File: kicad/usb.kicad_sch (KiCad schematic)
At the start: 0 parts

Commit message: added xu316
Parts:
- added U10: XU316-1024-QF60B-C24, QFN_F60B-C24_XMO, symbol openmic:XU316-1024-QF60B-C24
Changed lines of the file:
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@@
 	(generator_version "9.0")
 	(paper "A4")
+	(symbol
+		(lib_id "openmic:XU316-1024-QF60B-C24")
+		(at 123.19 57.15 0)
+		(unit 1)
+		(exclude_from_sim no)
+		(in_bom yes)
+		(on_board yes)
+		(dnp no)
+		(fields_autoplaced yes)
+		(property "Reference" "U10"
+			(at 151.13 46.99 0)
+			(effects
+				(font
+					(size 1.524 1.524)
+				)
+			)
+		)
+		(property "Value" "XU316-1024-QF60B-C24"
+			(at 151.13 49.53 0)
+			(effects
+				(font
+					(size 1.524 1.524)
+				)
+			)
+		)
+		(property "Footprint" "QFN_F60B-C24_XMO"
+			(at 123.19 57.15 0)
+			(effects
+				(font
+					(size 1.27 1.27)
+					(italic yes)
+				)
+				(hide yes)
+			)
+		)
+		(property "Datasheet" "XU316-1024-QF60B-C24"
+			(at 123.19 57.15 0)
+			(effects
+				(font
+					(size 1.27 1.27)
+					(italic yes)
+				)
+				(hide yes)
+			)
+		)
+		(property "Description" ""
+			(at 123.19 57.15 0)
+			(effects
+				(font
+					(size 1.27 1.27)
+				)
+				(hide yes)
+			)
+		)
+		(pin "17"
+		)
+		(pin "14"
+		)
+		(pin "16"
+		)
+		(pin "15"
+		)
+		(pin "56"
+		)
+		(pin "57"
+		)
+		(pin "58"
+		)
+		(pin "53"
+		)
+		(pin "54"
+		)
+		(pin "55"
+		)
+		(pin "59"
+		)
+		(pin "60"
+		)
+		(pin "39"
+		)
+		(pin "40"
+		)
+		(pin "38"
+		)
+		(pin "37"
+		)
+		(pin "35"
+		)
+		(pin "36"
+		)
+		(pin "33"
+		)
+		(pin "34"
+		)
+		(pin "25"
+		)
+		(pin "24"
+		)
+		(pin "23"
+		)
+		(pin "22"
+		)
+		(pin "6"
+		)
+		(pin "5"
+		)
+		(pin "13"
+		)
+		(pin "12"
+		)
+		(pin "1"
+		)
+		(pin "4"
+		)
+		(pin "3"
+		)
+		(pin "2"
+		)
+		(pin "10"
+		)
+		(pin "11"
+		)
+		(pin "9"
+		)
+		(pin "8"
+		)
+		(pin "7"
+		)
+		(pin "31"
+		)
+		(pin "30"
+		)
+		(pin "29"
+		)
+		(pin "28"
+		)
+		(pin "27"
+		)
+		(pin "26"
+		)
+		(pin "65"
+		)
+		(pin "32"
+		)
+		(pin "61"
+		)
+		(pin "62"
+		)
+		(pin "63"
+		)
+		(pin "64"
+		)
+		(pin "41"
+		)
+		(pin "52"
+		)
+		(pin "51"
+		)
+		(pin "50"
+		)
+		(pin "49"
+		)
+		(pin "48"
+		)
+		(pin "47"
+		)
+		(pin "46"
+		)
+		(pin "45"
+		)
+		(pin "44"
+		)
+		(pin "43"
+		)
+		(pin "42"
+		)
+		(pin "19"
+		)
+		(pin "18"
+		)
+		(pin "21"
+		)
+		(pin "20"
+		)
+		(instances
+			(project "openmic"
+				(path "/84faeadc-8b12-4a66-a17f-5c56e5923fb8/ac4749a9-b66d-4a3a-8eaa-94f1fe3c6a5c"
+					(reference "U10")
+					(unit 1)
+				)
+			)
+		)
+	)
 )

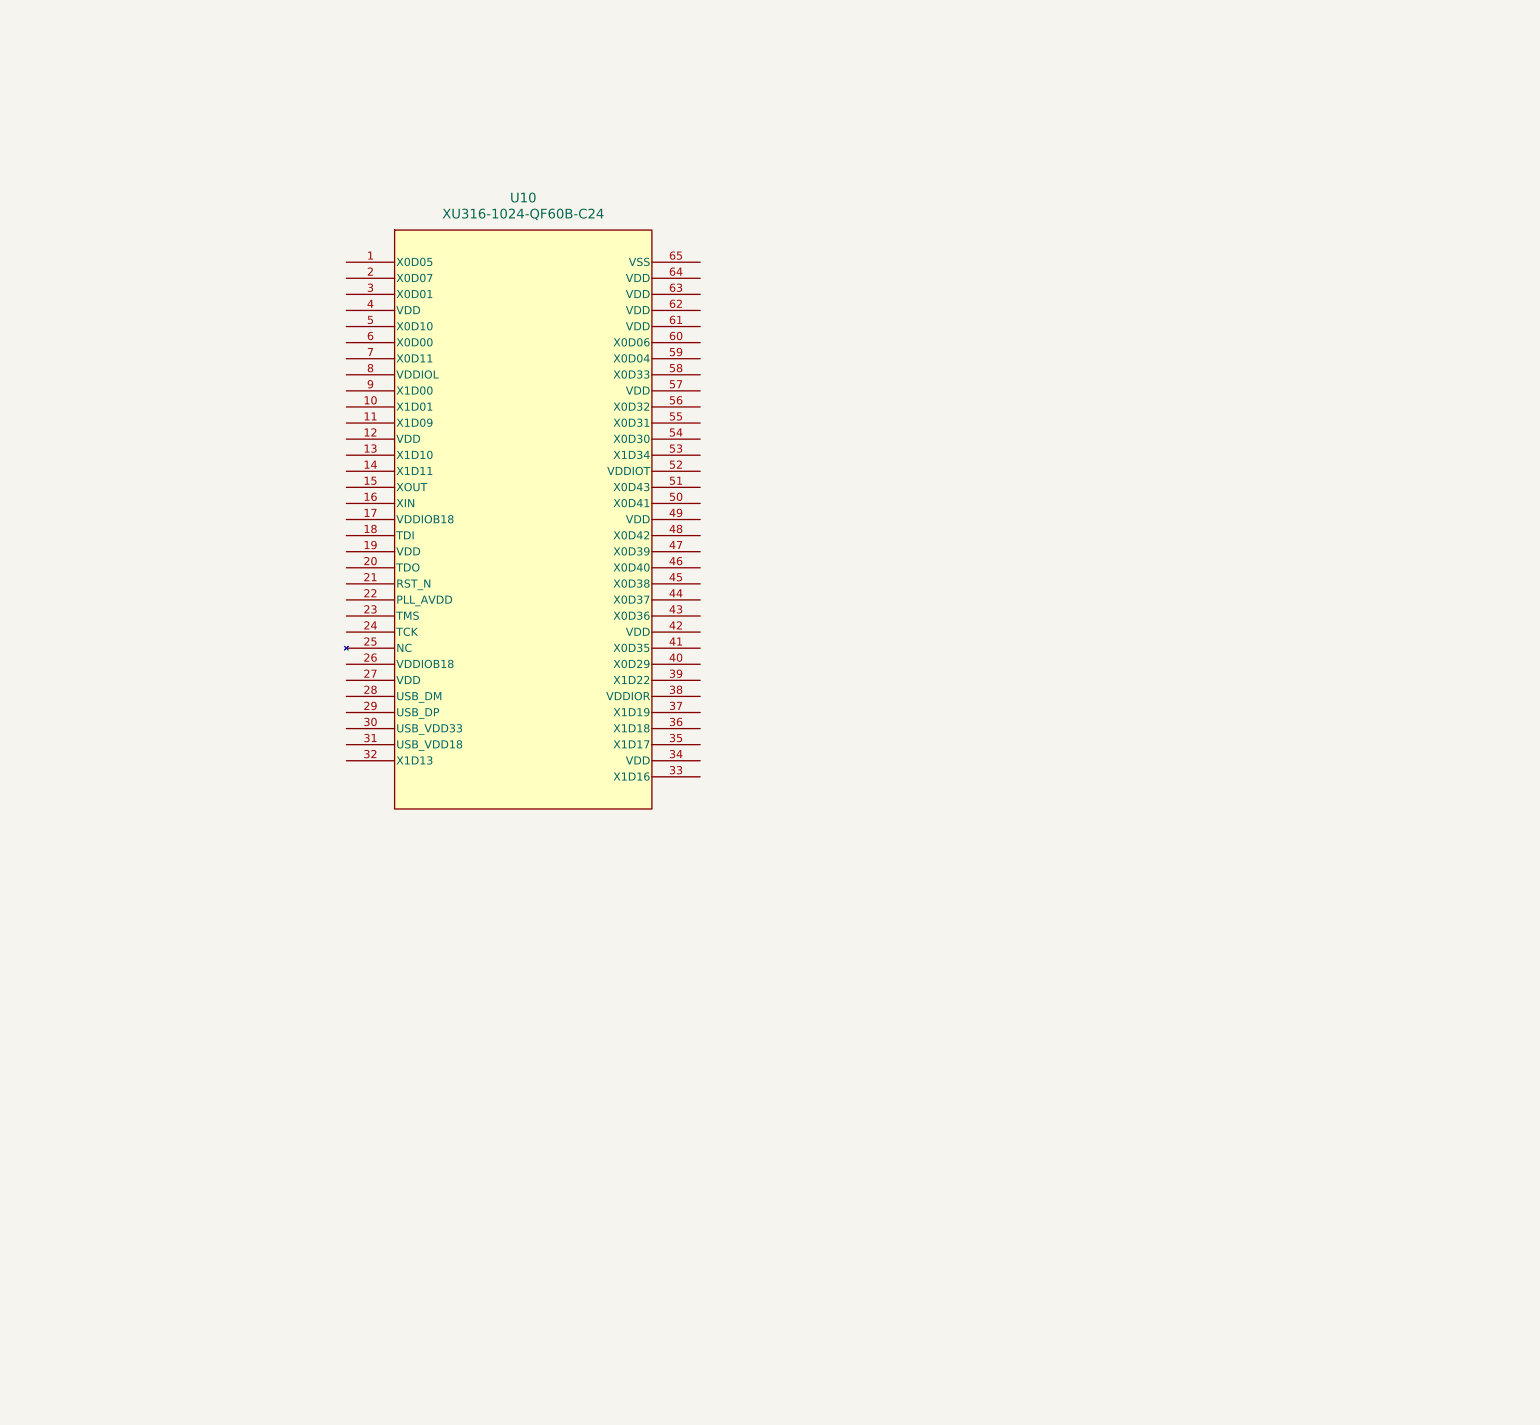
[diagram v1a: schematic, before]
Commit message: XU316 as usb device
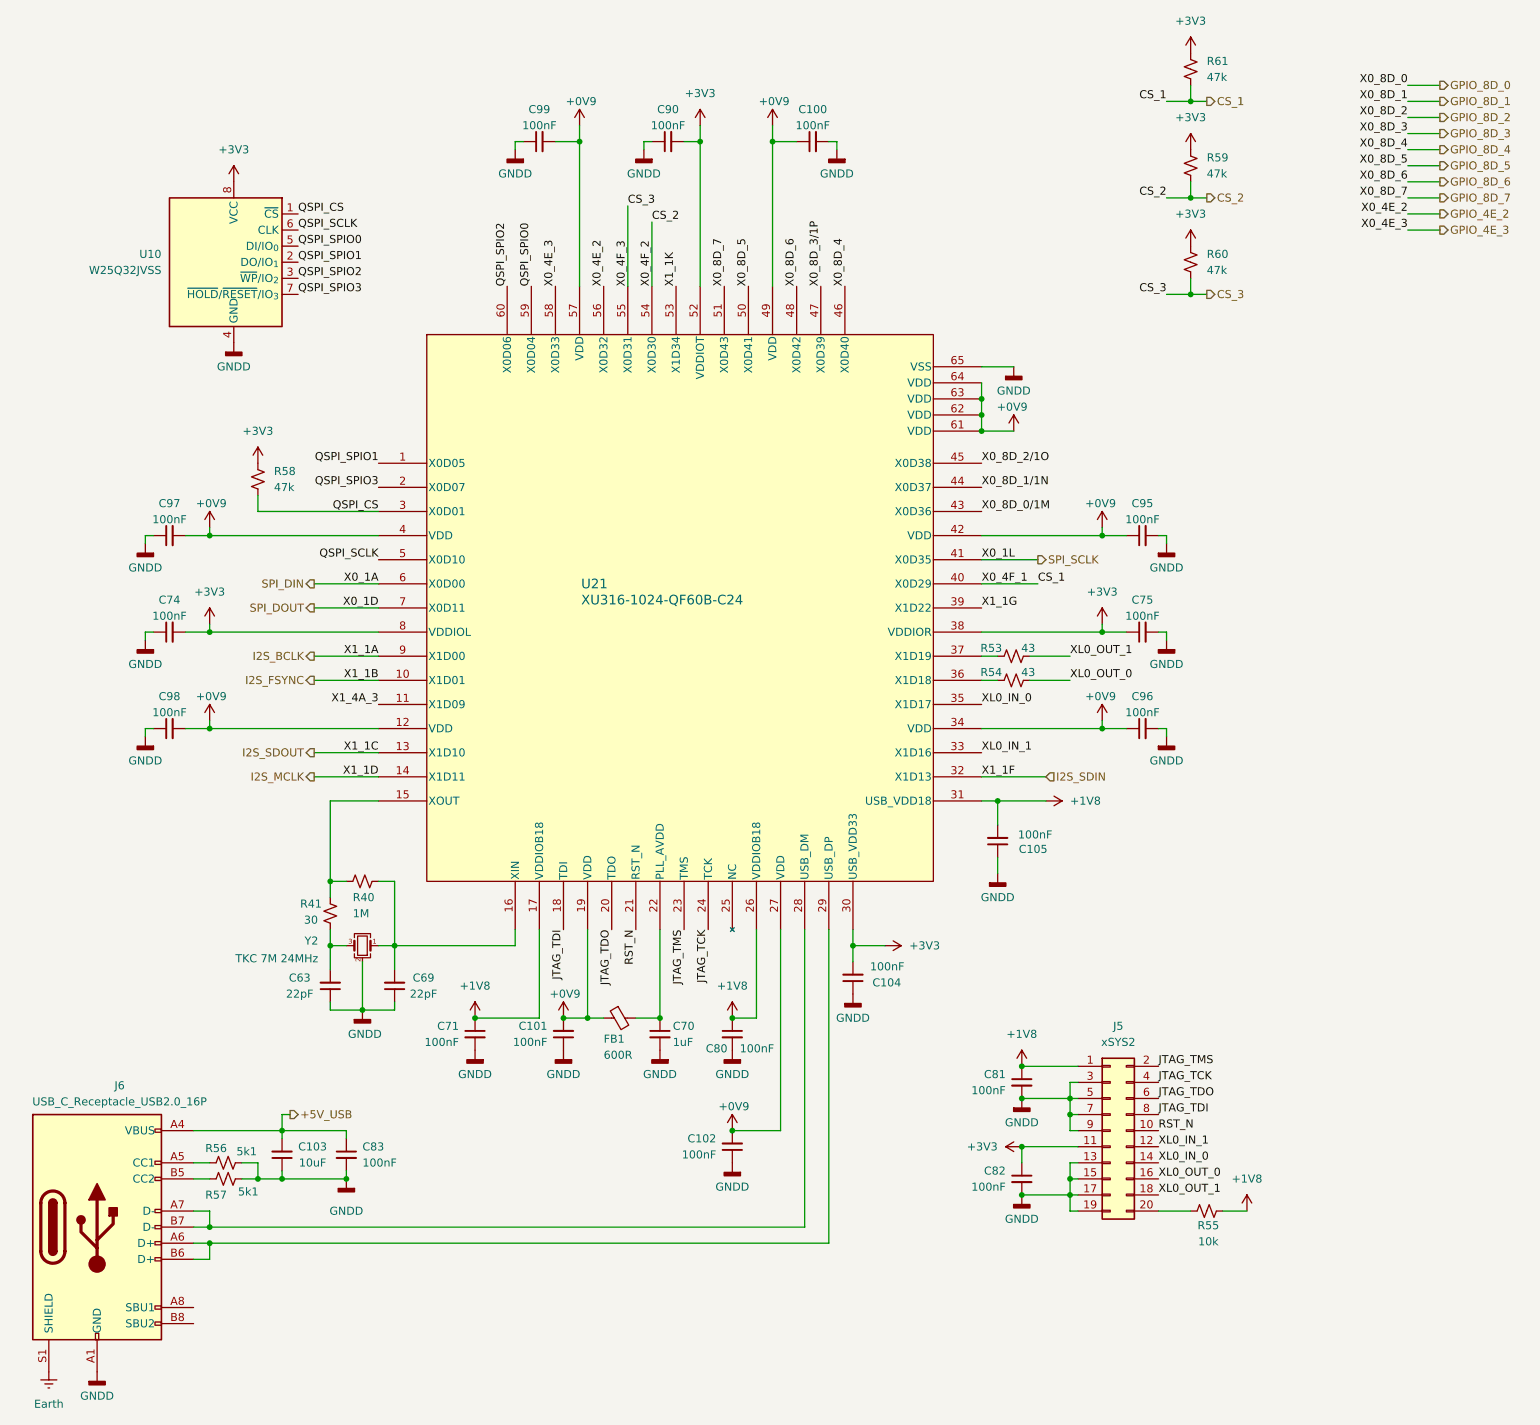
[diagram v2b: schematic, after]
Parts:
- removed U10: XU316-1024-QF60B-C24, QFN_F60B-C24_XMO, symbol openmic:XU316-1024-QF60B-C24
- added C100, C101, C102, C104, C105, C71, C74, C75, C80, C81, C82, C83, C90, C95, C96, C97, C98, C99: 100nF, symbol Device:C_Small
- added C103: 10uF, symbol Device:C_Small
- added C63, C69: 22pF, symbol Device:C_Small
- added C70: 1uF, symbol Device:C_Small
- added FB1: 600R, symbol Device:FerriteBead_Small
- added J5: xSYS2, symbol Connector_Generic:Conn_02x10_Odd_Even
- added J6: USB_C_Receptacle_USB2.0_16P, symbol Connector:USB_C_Receptacle_USB2.0_16P
- added R40: 1M, symbol Device:R_Small_US
- added R41: 30, symbol Device:R_Small_US
- added R53, R54: 43, symbol Device:R_Small_US
- added R55: 10k, symbol Device:R_Small_US
- added R56, R57: 5k1, symbol Device:R_Small_US
- added R58, R59, R60, R61: 47k, symbol Device:R_Small_US
- added U10: W25Q32JVSS, Package_SO:SOIC-8_5.3x5.3mm_P1.27mm, symbol Memory_Flash:W25Q32JVSS
- added U21: XU316-1024-QF60B-C24, QFN_F60B-C24_XMO, symbol openmic:XU316-1024-QF60B-C24_1
- added Y2: TKC 7M 24MHz, symbol Device:Crystal_GND24_Small
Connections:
- new net: C63.2, R41.1, Y2.3
- new net: J5.20 (Pin_20), R55.2
- new net: R40.1, R41.2, U21.15 (XOUT)
- new net: C69.2, R40.2, U21.16 (XIN), Y2.1
- new net: C70.1, FB1.2, U21.22 (PLL_AVDD)
- new net: J6.A7 (D-), J6.B7 (D-), U21.28 (USB_DM)
- new net: J6.A6 (D+), J6.B6 (D+), U21.29 (USB_DP)
- new net: R54.1, U21.36 (X1D18)
- new net: R53.1, U21.37 (X1D19)
- new net: J6.A5 (CC1), R56.1
- new net: J6.B5 (CC2), R57.2
- new net +0V9: C100.1, C101.2, C102.2, C95.1, C96.1, C97.2, C98.2, C99.2, FB1.1, U21.12 (VDD), U21.19 (VDD), U21.27 (VDD), U21.34 (VDD), U21.4 (VDD), U21.42 (VDD), U21.49 (VDD), U21.57 (VDD), U21.61 (VDD), U21.62 (VDD), U21.63 (VDD), U21.64 (VDD)
- new net +1V8: C105.2, C71.1, C80.1, C81.1, J5.1 (Pin_1), R55.1, U21.17 (VDDIOB18), U21.26 (VDDIOB18), U21.31 (USB_VDD18)
- new net +3V3: C104.2, C74.2, C75.1, C82.1, C90.2, J5.11 (Pin_11), R58.1, R59.1, R60.1, R61.1, U10.8 (VCC), U21.30 (USB_VDD33), U21.38 (VDDIOR), U21.52 (VDDIOT), U21.8 (VDDIOL)
- new net +5V_USB: C103.2, C83.1, J6.A4 (VBUS), J6.A9 (VBUS), J6.B4 (VBUS), J6.B9 (VBUS)
- new net CS_1: R61.2, U21.40 (X0D29)
- new net CS_2: R59.2, U21.54 (X0D30)
- new net CS_3: R60.2, U21.55 (X0D31)
- new net Earth: J6.S1 (SHIELD)
- new net GNDD: C100.2, C101.1, C102.1, C103.1, C104.1, C105.1, C63.1, C69.1, C70.2, C71.2, C74.1, C75.2, C80.2, C81.2, C82.2, C83.2, C90.1, C95.2, C96.2, C97.1, C98.1, C99.1, J5.13 (Pin_13), J5.15 (Pin_15), J5.17 (Pin_17), J5.19 (Pin_19), J5.3 (Pin_3), J5.5 (Pin_5), J5.7 (Pin_7), J5.9 (Pin_9), J6.A1 (GND), J6.A12 (GND), J6.B1 (GND), J6.B12 (GND), R56.2, R57.1, U10.4 (GND), U21.65 (VSS), Y2.2 (G), Y2.4 (G)
- new net GPIO_4E_2: U21.56 (X0D32)
- new net GPIO_4E_3: U21.58 (X0D33)
- new net GPIO_8D_4: U21.46 (X0D40)
- new net GPIO_8D_5: U21.50 (X0D41)
- new net GPIO_8D_6: U21.48 (X0D42)
- new net GPIO_8D_7: U21.51 (X0D43)
- new net I2S_BCLK: U21.9 (X1D00)
- new net I2S_FSYNC: U21.10 (X1D01)
- new net I2S_MCLK: U21.14 (X1D11)
- new net I2S_SDIN: U21.32 (X1D13)
- new net I2S_SDOUT: U21.13 (X1D10)
- new net JTAG_TCK: J5.4 (Pin_4), U21.24 (TCK)
- new net JTAG_TDI: J5.8 (Pin_8), U21.18 (TDI)
- new net JTAG_TDO: J5.6 (Pin_6), U21.20 (TDO)
- new net JTAG_TMS: J5.2 (Pin_2), U21.23 (TMS)
- new net QSPI_CS: R58.2, U10.1 (~{CS}), U21.3 (X0D01)
- new net QSPI_SCLK: U10.6 (CLK), U21.5 (X0D10)
- new net QSPI_SPIO0: U10.5 (DI/IO_{0}), U21.59 (X0D04)
- new net QSPI_SPIO1: U10.2 (DO/IO_{1}), U21.1 (X0D05)
- new net QSPI_SPIO2: U10.3 (~{WP}/IO_{2}), U21.60 (X0D06)
- new net QSPI_SPIO3: U10.7 (~{HOLD}/~{RESET}/IO_{3}), U21.2 (X0D07)
- new net RST_N: J5.10 (Pin_10), U21.21 (RST_N)
- new net SPI_DIN: U21.6 (X0D00)
- new net SPI_DOUT: U21.7 (X0D11)
- new net SPI_SCLK: U21.41 (X0D35)
- new net X0_8D_0/1M: U21.43 (X0D36)
- new net X0_8D_1/1N: U21.44 (X0D37)
- new net X0_8D_2/1O: U21.45 (X0D38)
- new net X0_8D_3/1P: U21.47 (X0D39)
- new net X1_1G: U21.39 (X1D22)
- new net X1_1K: U21.53 (X1D34)
- new net X1_4A_3: U21.11 (X1D09)
- new net XL0_IN_0: J5.14 (Pin_14), U21.35 (X1D17)
- new net XL0_IN_1: J5.12 (Pin_12), U21.33 (X1D16)
- new net XL0_OUT_0: J5.16 (Pin_16), R54.2
- new net XL0_OUT_1: J5.18 (Pin_18), R53.2

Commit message: rotary encoder
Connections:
- net GPIO_4E_2 renamed PH_EN
- net GPIO_8D_4 renamed ROT_B_2
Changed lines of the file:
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@@
+		)
+	)
+	(hierarchical_label "ROT_B_1"
+		(shape input)
+		(at 295.91 34.29 0)
+		(effects
+			(font
+				(size 1.27 1.27)
+			)
+			(justify left)
 		)
 	)
 	(hierarchical_label "GPIO_8D_7"
-		(shape output)
+		(shape input)
 		(at 295.91 46.99 0)
 		(effects
@@
 		)
 	)
+	(hierarchical_label "ROT_A_1"
+		(shape input)
+		(at 295.91 31.75 0)
+		(effects
+			(font
+				(size 1.27 1.27)
+			)
+			(justify left)
+		)
+	)
 	(hierarchical_label "CS_2"
 		(shape output)
@@
 		)
 	)
-	(hierarchical_label "GPIO_8D_3"
-		(shape output)
+	(hierarchical_label "SPI_DOUT"
+		(shape output)
+		(at 118.11 111.76 180)
+		(effects
+			(font
+				(size 1.27 1.27)
+			)
+			(justify right)
+		)
+	)
+	(hierarchical_label "I2S_SDOUT"
+		(shape output)
+		(at 118.11 134.62 180)
+		(effects
+			(font
+				(size 1.27 1.27)
+			)
+			(justify right)
+		)
+	)
+	(hierarchical_label "CS_3"
+		(shape output)
+		(at 259.08 62.23 0)
+		(effects
+			(font
+				(size 1.27 1.27)
+			)
+			(justify left)
+		)
+	)
+	(hierarchical_label "GPIO_8D_6"
+		(shape input)
+		(at 295.91 44.45 0)
+		(effects
+			(font
+				(size 1.27 1.27)
+			)
+			(justify left)
+		)
+	)
+	(hierarchical_label "SPI_SCLK"
+		(shape output)
+		(at 232.41 104.14 0)
+		(effects
+			(font
+				(size 1.27 1.27)
+			)
+			(justify left)
+		)
+	)
+	(hierarchical_label "PH_IND"
+		(shape input)
+		(at 295.91 29.21 0)
+		(effects
+			(font
+				(size 1.27 1.27)
+			)
+			(justify left)
+		)
+	)
+	(hierarchical_label "GPIO_8D_5"
+		(shape input)
+		(at 295.91 41.91 0)
+		(effects
+			(font
+				(size 1.27 1.27)
+			)
+			(justify left)
+		)
+	)
+	(hierarchical_label "+5V_USB"
+		(shape output)
+		(at 114.3 191.77 0)
+		(effects
+			(font
+				(size 1.27 1.27)
+			)
+			(justify left)
+		)
+	)
+	(hierarchical_label "I2S_FSYNC"
+		(shape output)
+		(at 118.11 123.19 180)
+		(effects
+			(font
+				(size 1.27 1.27)
+			)
+			(justify right)
+		)
+	)
+	(hierarchical_label "SPI_DIN"
+		(shape output)
+		(at 118.11 107.95 180)
+		(effects
+			(font
+				(size 1.27 1.27)
+			)
+			(justify right)
+		)
+	)
+	(hierarchical_label "ROT_B_2"
+		(shape input)
+		(at 295.91 39.37 0)
+		(effects
+			(font
+				(size 1.27 1.27)
+			)
+			(justify left)
+		)
+	)
+	(hierarchical_label "PH_EN"
+		(shape output)
+		(at 295.91 49.53 0)
+		(effects
+			(font
+				(size 1.27 1.27)
+			)
+			(justify left)
+		)
+	)
+	(hierarchical_label "ROT_A_2"
+		(shape input)
 		(at 295.91 36.83 0)
 		(effects
 			(font
-				(size 1.27 1.27)
-			)
-			(justify left)
-		)
-	)
-	(hierarchical_label "GPIO_8D_1"
-		(shape output)
-		(at 295.91 31.75 0)
-		(effects
-			(font
-				(size 1.27 1.27)
-			)
-			(justify left)
-		)
-	)
-	(hierarchical_label "GPIO_8D_2"
-		(shape output)
-		(at 295.91 34.29 0)
-		(effects
-			(font
-				(size 1.27 1.27)
-			)
-			(justify left)
-		)
-	)
-	(hierarchical_label "GPIO_8D_4"
-		(shape output)
-		(at 295.91 39.37 0)
-		(effects
-			(font
-				(size 1.27 1.27)
-			)
-			(justify left)
-		)
-	)
-	(hierarchical_label "SPI_DOUT"
-		(shape output)
-		(at 118.11 111.76 180)
-		(effects
-			(font
-				(size 1.27 1.27)
-			)
-			(justify right)
-		)
-	)
-	(hierarchical_label "I2S_SDOUT"
-		(shape output)
-		(at 118.11 134.62 180)
-		(effects
-			(font
-				(size 1.27 1.27)
-			)
-			(justify right)
-		)
-	)
-	(hierarchical_label "CS_3"
-		(shape output)
-		(at 259.08 62.23 0)
-		(effects
-			(font
-				(size 1.27 1.27)
-			)
-			(justify left)
-		)
-	)
-	(hierarchical_label "GPIO_8D_6"
-		(shape output)
-		(at 295.91 44.45 0)
-		(effects
-			(font
-				(size 1.27 1.27)
-			)
-			(justify left)
-		)
-	)
-	(hierarchical_label "SPI_SCLK"
-		(shape output)
-		(at 232.41 104.14 0)
-		(effects
-			(font
-				(size 1.27 1.27)
-			)
-			(justify left)
-		)
-	)
-	(hierarchical_label "GPIO_8D_0"
-		(shape output)
-		(at 295.91 29.21 0)
-		(effects
-			(font
-				(size 1.27 1.27)
-			)
-			(justify left)
-		)
-	)
-	(hierarchical_label "GPIO_8D_5"
-		(shape output)
-		(at 295.91 41.91 0)
-		(effects
-			(font
-				(size 1.27 1.27)
-			)
-			(justify left)
-		)
-	)
-	(hierarchical_label "+5V_USB"
-		(shape output)
-		(at 114.3 191.77 0)
-		(effects
-			(font
-				(size 1.27 1.27)
-			)
-			(justify left)
-		)
-	)
-	(hierarchical_label "I2S_FSYNC"
-		(shape output)
-		(at 118.11 123.19 180)
-		(effects
-			(font
-				(size 1.27 1.27)
-			)
-			(justify right)
-		)
-	)
-	(hierarchical_label "SPI_DIN"
-		(shape output)
-		(at 118.11 107.95 180)
-		(effects
-			(font
-				(size 1.27 1.27)
-			)
-			(justify right)
-		)
-	)
-	(hierarchical_label "GPIO_4E_2"
-		(shape output)
-		(at 295.91 49.53 0)
-		(effects
-			(font
